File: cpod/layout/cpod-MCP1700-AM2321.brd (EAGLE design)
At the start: 13 parts

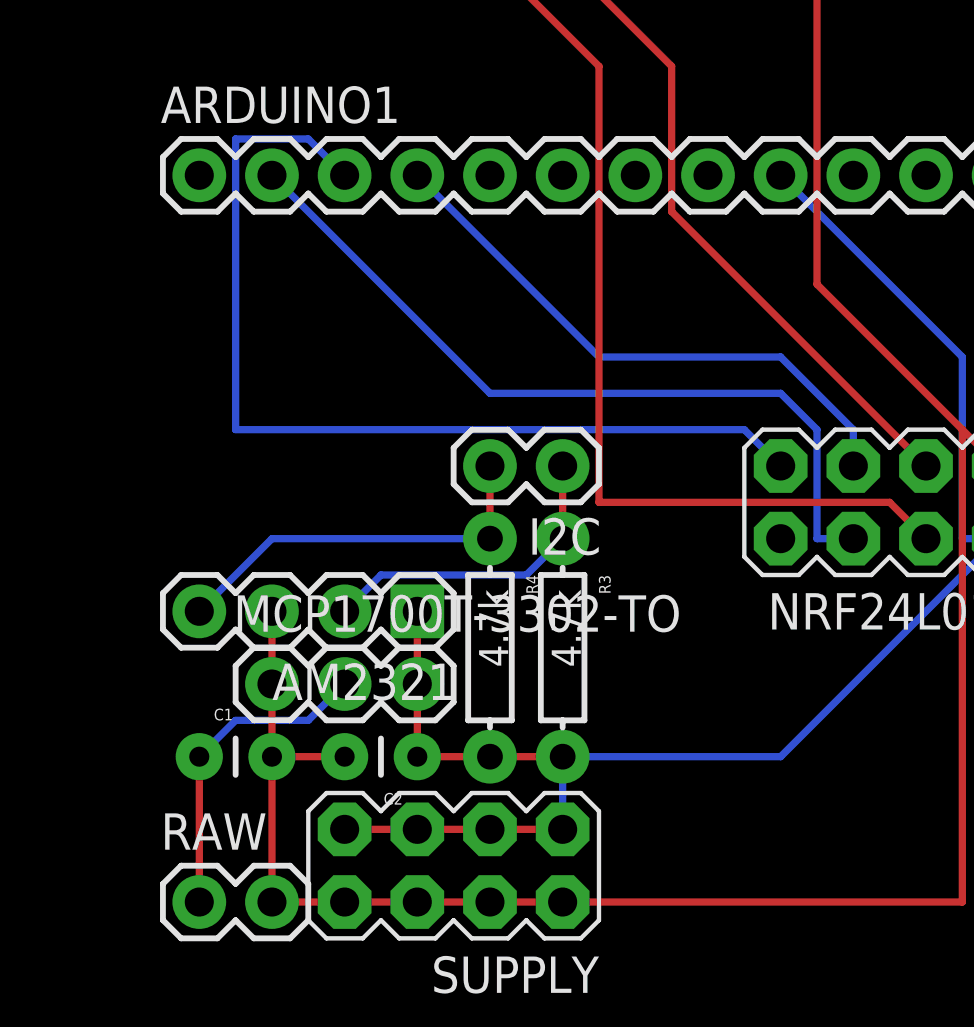
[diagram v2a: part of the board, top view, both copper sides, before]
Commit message: 改为单总线
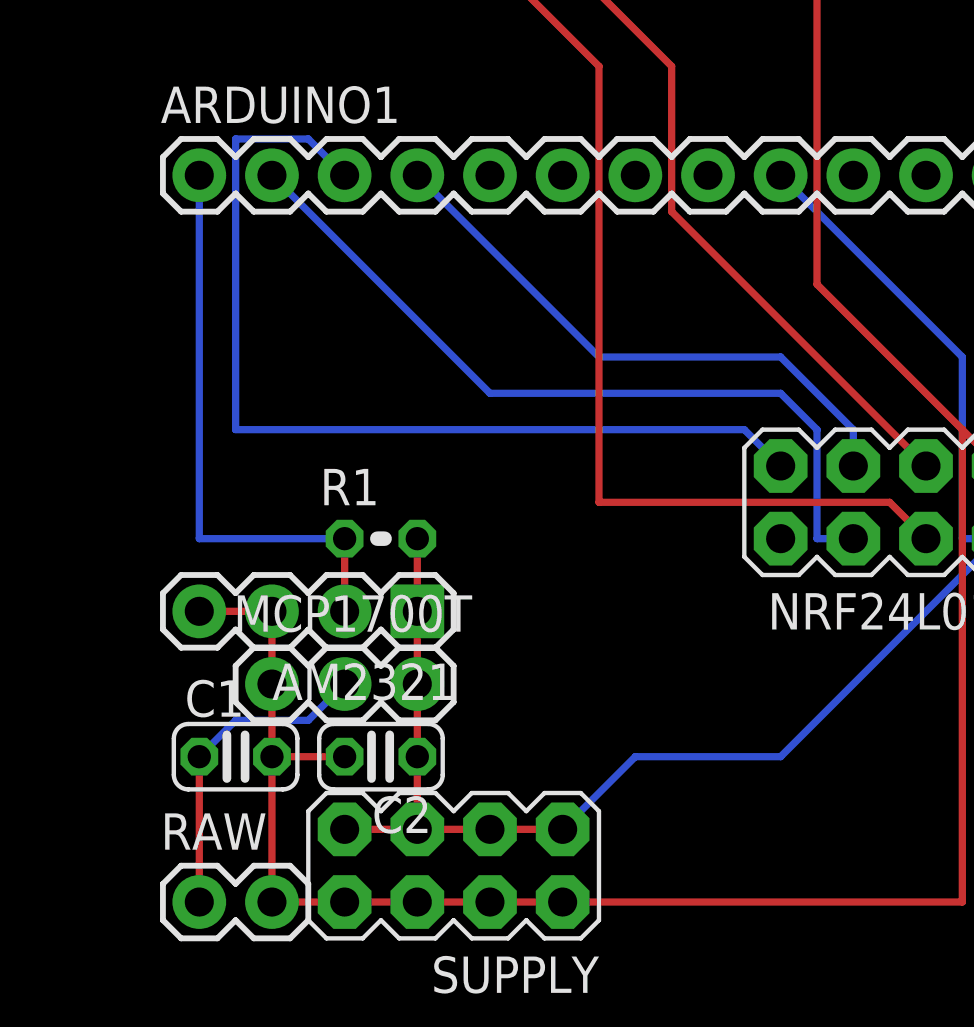
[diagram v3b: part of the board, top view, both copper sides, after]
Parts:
- removed I2C: (no value), SparkFun-Connectors:1X02
- removed R3, R4: 4.7k, SparkFun-Resistors:AXIAL-0.3
- added R1: 5.1k, rcl:0204V
- C1, C2: device SparkFun-Capacitors:CAP-PTH-SMALL -> rcl:C025-024X044
- MCP1700T: value (none) -> +3V3
- moved C1 1.27 mm to (33.0, -36.8)
- moved C2 1.27 mm to (38.1, -36.8)
- renumbered MCP1700T-3302-TO to MCP1700T
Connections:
- removed net D10: ARDUINO1.1
- removed net SCL: AM2321.4, I2C.2, R4.P$1
- net GND: now also AM2321.4
- net SDA: now also ARDUINO1.1, R1.1; no longer I2C.1, R3.P$1
- net VCC: now also R1.2; no longer R3.P$2, R4.P$2
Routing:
- net SCL: track 13.8 -> 0.00 mm
- net SDA: track 11.2 -> 20.3 mm
- net GND: track 81.9 -> 84.4 mm
- net VCC: track 55.3 -> 53.8 mm
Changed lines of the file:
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@@
 <setting verticaltext="up"/>
 </settings>
-<grid distance="0.1" unitdist="inch" unit="inch" style="lines" multiple="1" display="yes" altdistance="0.05" altunitdist="inch" altunit="inch"/>
+<grid distance="0.1" unitdist="inch" unit="inch" style="dots" multiple="1" display="yes" altdistance="0.05" altunitdist="inch" altunit="inch"/>
 <layers>
 <layer number="1" name="Top" color="4" fill="1" visible="yes" active="yes"/>
@@
 <elements>
 <element name="AM2321" library="SparkFun-Connectors" package="1X04" value="" x="39.37" y="-31.75" rot="R180"/>
-<element name="MCP1700T-3302-TO" library="SparkFun-Connectors" package="1X03" value="" x="34.29" y="-34.29"/>
-<element name="C1" library="SparkFun-Capacitors" package="CAP-PTH-SMALL" value="1uF" x="31.75" y="-36.83"/>
-<element name="C2" library="SparkFun-Capacitors" package="CAP-PTH-SMALL" value="1uF" x="39.37" y="-36.83" rot="R180"/>
+<element name="MCP1700T" library="SparkFun-Connectors" package="1X03" value="+3V3" x="34.29" y="-34.29"/>
 <element name="ARDUINO1" library="SparkFun-Connectors" package="1X12" value="M12PTH" x="31.75" y="-16.51"/>
 <element name="ARDUINO2" library="SparkFun-Connectors" package="1X12" value="M12PTH" x="31.75" y="-1.27"/>
 <element name="RAW" library="SparkFun-Connectors" package="1X02" value="" x="31.75" y="-41.91"/>
 <element name="NRF24L01+" library="SparkFun-Connectors" package="2X4" value="M04X2" x="55.88" y="-27.94" rot="R180"/>
-<element name="R3" library="SparkFun-Resistors" package="AXIAL-0.3" value="4.7k" x="44.45" y="-33.02" rot="R270"/>
-<element name="R4" library="SparkFun-Resistors" package="AXIAL-0.3" value="4.7k" x="41.91" y="-33.02" rot="R270"/>
-<element name="I2C" library="SparkFun-Connectors" package="1X02" value="" x="44.45" y="-26.67" rot="R180"/>
 <element name="SUPPLY" library="SparkFun-Connectors" package="2X4" value="M04X2" x="40.64" y="-40.64" rot="R180"/>
 <element name="U$2" library="SparkFun-Aesthetics" package="OSHW-LOGO-L" value="" x="5.08" y="-38.1"/>
+<element name="R1" library="rcl" package="0204V" value="5.1k" x="38.1" y="-29.21"/>
+<element name="C1" library="rcl" package="C025-024X044" value="1uF" x="33.02" y="-36.83"/>
+<element name="C2" library="rcl" package="C025-024X044" value="1uF" x="38.1" y="-36.83" rot="R180"/>
 </elements>
 <signals>
-<signal name="SCL">
-<contactref element="AM2321" pad="4"/>
-<contactref element="I2C" pad="2"/>
-<contactref element="R4" pad="P$1"/>
-<wire x1="34.29" y1="-29.21" x2="31.75" y2="-31.75" width="0.254" layer="16"/>
-<wire x1="41.91" y1="-29.21" x2="34.29" y2="-29.21" width="0.254" layer="16"/>
-<wire x1="41.91" y1="-29.21" x2="41.91" y2="-26.67" width="0.254" layer="1"/>
-</signal>
 <signal name="GND">
-<contactref element="MCP1700T-3302-TO" pad="1"/>
+<contactref element="MCP1700T" pad="1"/>
 <contactref element="ARDUINO2" pad="9"/>
-<contactref element="C1" pad="2"/>
-<contactref element="C2" pad="2"/>
 <contactref element="AM2321" pad="3"/>
 <contactref element="RAW" pad="2"/>
@@
 <contactref element="SUPPLY" pad="6"/>
 <contactref element="NRF24L01+" pad="1"/>
-<wire x1="34.29" y1="-34.29" x2="34.29" y2="-36.83" width="0.254" layer="1"/>
-<wire x1="34.29" y1="-36.83" x2="36.83" y2="-36.83" width="0.254" layer="1"/>
 <wire x1="34.29" y1="-34.29" x2="34.29" y2="-31.75" width="0.254" layer="1"/>
 <wire x1="36.83" y1="-41.91" x2="34.29" y2="-41.91" width="0.254" layer="1"/>
@@
 <wire x1="39.37" y1="-41.91" x2="41.91" y2="-41.91" width="0.254" layer="1"/>
 <wire x1="41.91" y1="-41.91" x2="44.45" y2="-41.91" width="0.254" layer="1"/>
-<wire x1="34.29" y1="-41.91" x2="34.29" y2="-36.83" width="0.254" layer="1"/>
 <wire x1="53.34" y1="-20.32" x2="58.42" y2="-25.4" width="0.254" layer="1"/>
 <wire x1="58.42" y1="-25.4" x2="59.69" y2="-26.67" width="0.254" layer="1"/>
@@
 <wire x1="58.42" y1="-41.91" x2="44.45" y2="-41.91" width="0.254" layer="1"/>
 <wire x1="58.42" y1="-25.4" x2="58.42" y2="-41.91" width="0.254" layer="1"/>
+<contactref element="AM2321" pad="4"/>
+<wire x1="34.29" y1="-31.75" x2="31.75" y2="-31.75" width="0.254" layer="1"/>
+<contactref element="C1" pad="2"/>
+<contactref element="C2" pad="2"/>
+<wire x1="34.29" y1="-34.29" x2="34.29" y2="-36.83" width="0.254" layer="1"/>
+<wire x1="34.29" y1="-36.83" x2="36.83" y2="-36.83" width="0.254" layer="1"/>
+<wire x1="34.29" y1="-41.91" x2="34.29" y2="-36.83" width="0.254" layer="1"/>
 </signal>
 <signal name="SDA">
 <contactref element="AM2321" pad="2"/>
-<contactref element="I2C" pad="1"/>
-<contactref element="R3" pad="P$1"/>
-<wire x1="38.1" y1="-30.48" x2="36.83" y2="-31.75" width="0.254" layer="16"/>
-<wire x1="43.18" y1="-30.48" x2="38.1" y2="-30.48" width="0.254" layer="16"/>
-<wire x1="44.45" y1="-29.21" x2="43.18" y2="-30.48" width="0.254" layer="16"/>
-<wire x1="44.45" y1="-29.21" x2="44.45" y2="-26.67" width="0.254" layer="1"/>
+<contactref element="R1" pad="1"/>
+<wire x1="36.83" y1="-31.75" x2="36.83" y2="-29.21" width="0.254" layer="1"/>
+<contactref element="ARDUINO1" pad="1"/>
+<wire x1="31.75" y1="-16.51" x2="31.75" y2="-29.21" width="0.254" layer="16"/>
+<wire x1="31.75" y1="-29.21" x2="36.83" y2="-29.21" width="0.254" layer="16"/>
 </signal>
 <signal name="VCC">
 <contactref element="AM2321" pad="1"/>
 <contactref element="ARDUINO1" pad="9"/>
-<contactref element="C2" pad="1"/>
-<contactref element="R4" pad="P$2"/>
-<contactref element="R3" pad="P$2"/>
 <contactref element="SUPPLY" pad="1"/>
 <contactref element="SUPPLY" pad="7"/>
@@
 <contactref element="SUPPLY" pad="3"/>
 <contactref element="NRF24L01+" pad="2"/>
-<contactref element="MCP1700T-3302-TO" pad="3"/>
 <wire x1="39.37" y1="-39.37" x2="36.83" y2="-39.37" width="0.254" layer="1"/>
 <wire x1="39.37" y1="-39.37" x2="41.91" y2="-39.37" width="0.254" layer="1"/>
 <wire x1="41.91" y1="-39.37" x2="44.45" y2="-39.37" width="0.254" layer="1"/>
-<wire x1="39.37" y1="-34.29" x2="39.37" y2="-36.83" width="0.254" layer="1"/>
-<wire x1="39.37" y1="-34.29" x2="39.37" y2="-31.75" width="0.254" layer="1"/>
-<wire x1="39.37" y1="-36.83" x2="41.91" y2="-36.83" width="0.254" layer="1"/>
-<wire x1="41.91" y1="-36.83" x2="44.45" y2="-36.83" width="0.254" layer="1"/>
 <wire x1="52.07" y1="-36.83" x2="59.69" y2="-29.21" width="0.254" layer="16"/>
-<wire x1="44.45" y1="-36.83" x2="52.07" y2="-36.83" width="0.254" layer="16"/>
 <wire x1="58.42" y1="-22.86" x2="52.07" y2="-16.51" width="0.254" layer="16"/>
 <wire x1="58.42" y1="-29.21" x2="58.42" y2="-22.86" width="0.254" layer="16"/>
 <wire x1="59.69" y1="-29.21" x2="58.42" y2="-29.21" width="0.254" layer="16"/>
-<wire x1="44.45" y1="-36.83" x2="44.45" y2="-39.37" width="0.254" layer="16"/>
+<contactref element="R1" pad="2"/>
+<wire x1="39.37" y1="-31.75" x2="39.37" y2="-29.21" width="0.254" layer="1"/>
+<wire x1="46.99" y1="-36.83" x2="44.45" y2="-39.37" width="0.254" layer="16"/>
+<wire x1="52.07" y1="-36.83" x2="46.99" y2="-36.83" width="0.254" layer="16"/>
+<contactref element="C2" pad="1"/>
+<wire x1="39.37" y1="-39.37" x2="39.37" y2="-36.83" width="0.254" layer="1"/>
+<contactref element="MCP1700T" pad="3"/>
+<wire x1="39.37" y1="-31.75" x2="39.37" y2="-34.29" width="0.254" layer="1"/>
+<wire x1="39.37" y1="-36.83" x2="39.37" y2="-34.29" width="0.254" layer="1"/>
 </signal>
 <signal name="RAW">
-<contactref element="MCP1700T-3302-TO" pad="2"/>
-<contactref element="C1" pad="1"/>
+<contactref element="MCP1700T" pad="2"/>
 <contactref element="RAW" pad="1"/>
-<wire x1="31.75" y1="-41.91" x2="31.75" y2="-36.83" width="0.254" layer="1"/>
 <wire x1="35.56" y1="-35.56" x2="36.83" y2="-34.29" width="0.254" layer="16"/>
 <wire x1="33.02" y1="-35.56" x2="35.56" y2="-35.56" width="0.254" layer="16"/>
-<wire x1="31.75" y1="-36.83" x2="33.02" y2="-35.56" width="0.254" layer="16"/>
+<contactref element="C1" pad="1"/>
+<wire x1="33.02" y1="-35.56" x2="31.75" y2="-36.83" width="0.254" layer="16"/>
+<wire x1="31.75" y1="-41.91" x2="31.75" y2="-36.83" width="0.254" layer="1"/>
 </signal>
 <signal name="AD3">
@@
 <wire x1="54.61" y1="-29.21" x2="53.34" y2="-29.21" width="0.254" layer="16"/>
 </signal>
-<signal name="D10">
-<contactref element="ARDUINO1" pad="1"/>
-</signal>
 <signal name="TX">

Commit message: 留出了电解电容的位置
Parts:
- moved R1 5.08 mm to (38.1, -24.1)
- moved AM2321 5.08 mm to (39.4, -26.7)
- moved MCP1700T 5.08 mm to (34.3, -29.2)
- moved C1 2.54 mm to (33.0, -34.3)
- moved C2 2.54 mm to (38.1, -34.3)
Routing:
- net GND: track 84.4 -> 89.5 mm
- net VCC: track 53.8 -> 58.9 mm
- net SDA: track 20.3 -> 15.2 mm
- net RAW: track 11.2 -> 14.8 mm
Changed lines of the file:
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@@
 </autorouter>
 <elements>
-<element name="AM2321" library="SparkFun-Connectors" package="1X04" value="" x="39.37" y="-31.75" rot="R180"/>
-<element name="MCP1700T" library="SparkFun-Connectors" package="1X03" value="+3V3" x="34.29" y="-34.29"/>
+<element name="AM2321" library="SparkFun-Connectors" package="1X04" value="" x="39.37" y="-26.67" rot="R180"/>
+<element name="MCP1700T" library="SparkFun-Connectors" package="1X03" value="+3V3" x="34.29" y="-29.21"/>
 <element name="ARDUINO1" library="SparkFun-Connectors" package="1X12" value="M12PTH" x="31.75" y="-16.51"/>
 <element name="ARDUINO2" library="SparkFun-Connectors" package="1X12" value="M12PTH" x="31.75" y="-1.27"/>
@@
 <element name="SUPPLY" library="SparkFun-Connectors" package="2X4" value="M04X2" x="40.64" y="-40.64" rot="R180"/>
 <element name="U$2" library="SparkFun-Aesthetics" package="OSHW-LOGO-L" value="" x="5.08" y="-38.1"/>
-<element name="R1" library="rcl" package="0204V" value="5.1k" x="38.1" y="-29.21"/>
-<element name="C1" library="rcl" package="C025-024X044" value="1uF" x="33.02" y="-36.83"/>
-<element name="C2" library="rcl" package="C025-024X044" value="1uF" x="38.1" y="-36.83" rot="R180"/>
+<element name="R1" library="rcl" package="0204V" value="5.1k" x="38.1" y="-24.13"/>
+<element name="C1" library="rcl" package="C025-024X044" value="1uF" x="33.02" y="-34.29"/>
+<element name="C2" library="rcl" package="C025-024X044" value="1uF" x="38.1" y="-34.29" rot="R180"/>
 </elements>
 <signals>
@@
 <contactref element="SUPPLY" pad="6"/>
 <contactref element="NRF24L01+" pad="1"/>
-<wire x1="34.29" y1="-34.29" x2="34.29" y2="-31.75" width="0.254" layer="1"/>
+<wire x1="34.29" y1="-29.21" x2="34.29" y2="-26.67" width="0.254" layer="1"/>
 <wire x1="36.83" y1="-41.91" x2="34.29" y2="-41.91" width="0.254" layer="1"/>
 <wire x1="36.83" y1="-41.91" x2="39.37" y2="-41.91" width="0.254" layer="1"/>
@@
 <wire x1="58.42" y1="-25.4" x2="58.42" y2="-41.91" width="0.254" layer="1"/>
 <contactref element="AM2321" pad="4"/>
-<wire x1="34.29" y1="-31.75" x2="31.75" y2="-31.75" width="0.254" layer="1"/>
+<wire x1="34.29" y1="-26.67" x2="31.75" y2="-26.67" width="0.254" layer="1"/>
 <contactref element="C1" pad="2"/>
 <contactref element="C2" pad="2"/>
-<wire x1="34.29" y1="-34.29" x2="34.29" y2="-36.83" width="0.254" layer="1"/>
-<wire x1="34.29" y1="-36.83" x2="36.83" y2="-36.83" width="0.254" layer="1"/>
-<wire x1="34.29" y1="-41.91" x2="34.29" y2="-36.83" width="0.254" layer="1"/>
+<wire x1="34.29" y1="-29.21" x2="34.29" y2="-34.29" width="0.254" layer="1"/>
+<wire x1="34.29" y1="-34.29" x2="36.83" y2="-34.29" width="0.254" layer="1"/>
+<wire x1="34.29" y1="-41.91" x2="34.29" y2="-34.29" width="0.254" layer="1"/>
 </signal>
 <signal name="SDA">
 <contactref element="AM2321" pad="2"/>
 <contactref element="R1" pad="1"/>
-<wire x1="36.83" y1="-31.75" x2="36.83" y2="-29.21" width="0.254" layer="1"/>
+<wire x1="36.83" y1="-26.67" x2="36.83" y2="-24.13" width="0.254" layer="1"/>
 <contactref element="ARDUINO1" pad="1"/>
-<wire x1="31.75" y1="-16.51" x2="31.75" y2="-29.21" width="0.254" layer="16"/>
-<wire x1="31.75" y1="-29.21" x2="36.83" y2="-29.21" width="0.254" layer="16"/>
+<wire x1="31.75" y1="-16.51" x2="31.75" y2="-24.13" width="0.254" layer="1"/>
+<wire x1="31.75" y1="-24.13" x2="36.83" y2="-24.13" width="0.254" layer="1"/>
 </signal>
 <signal name="VCC">
@@
 <wire x1="59.69" y1="-29.21" x2="58.42" y2="-29.21" width="0.254" layer="16"/>
 <contactref element="R1" pad="2"/>
-<wire x1="39.37" y1="-31.75" x2="39.37" y2="-29.21" width="0.254" layer="1"/>
+<wire x1="39.37" y1="-26.67" x2="39.37" y2="-24.13" width="0.254" layer="1"/>
 <wire x1="46.99" y1="-36.83" x2="44.45" y2="-39.37" width="0.254" layer="16"/>
 <wire x1="52.07" y1="-36.83" x2="46.99" y2="-36.83" width="0.254" layer="16"/>
 <contactref element="C2" pad="1"/>
-<wire x1="39.37" y1="-39.37" x2="39.37" y2="-36.83" width="0.254" layer="1"/>
+<wire x1="39.37" y1="-39.37" x2="39.37" y2="-34.29" width="0.254" layer="1"/>
 <contactref element="MCP1700T" pad="3"/>
-<wire x1="39.37" y1="-31.75" x2="39.37" y2="-34.29" width="0.254" layer="1"/>
-<wire x1="39.37" y1="-36.83" x2="39.37" y2="-34.29" width="0.254" layer="1"/>
+<wire x1="39.37" y1="-26.67" x2="39.37" y2="-29.21" width="0.254" layer="1"/>
+<wire x1="39.37" y1="-34.29" x2="39.37" y2="-29.21" width="0.254" layer="1"/>
 </signal>
 <signal name="RAW">
 <contactref element="MCP1700T" pad="2"/>
 <contactref element="RAW" pad="1"/>
-<wire x1="35.56" y1="-35.56" x2="36.83" y2="-34.29" width="0.254" layer="16"/>
-<wire x1="33.02" y1="-35.56" x2="35.56" y2="-35.56" width="0.254" layer="16"/>
+<wire x1="31.75" y1="-34.29" x2="36.83" y2="-29.21" width="0.254" layer="16"/>
 <contactref element="C1" pad="1"/>
-<wire x1="33.02" y1="-35.56" x2="31.75" y2="-36.83" width="0.254" layer="16"/>
-<wire x1="31.75" y1="-41.91" x2="31.75" y2="-36.83" width="0.254" layer="1"/>
+<wire x1="31.75" y1="-41.91" x2="31.75" y2="-34.29" width="0.254" layer="1"/>
 </signal>
 <signal name="AD3">
